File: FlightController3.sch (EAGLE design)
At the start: 38 parts, among them U1 NUCLEO_L432KC

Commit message: various improvements, mostly silkscreen labels
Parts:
- C13, C14: value (none) -> I2C
- C2: value AILERON_L -> AILERON L
- C3: value V_TAIL_L -> V-TAIL L
- C4: value V_TAIL_R -> V-TAIL R
- C5: value AILERON_R -> AILERON R
- INS1: value BNO055-BREAKOUT -> BNO055
- JP1, S1: value (none) -> RESET
- LED1: value (none) -> 5V
- LED2: value (none) -> 3V3
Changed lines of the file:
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@@
 <parts>
 <part name="C1" library="pinhead" deviceset="PINHD-1X3" device="" value="MOTOR"/>
-<part name="C2" library="pinhead" deviceset="PINHD-1X3" device="" value="AILERON_L"/>
-<part name="C5" library="pinhead" deviceset="PINHD-1X3" device="" value="AILERON_R"/>
-<part name="C3" library="pinhead" deviceset="PINHD-1X3" device="" value="V_TAIL_L"/>
-<part name="C4" library="pinhead" deviceset="PINHD-1X3" device="" value="V_TAIL_R"/>
+<part name="C2" library="pinhead" deviceset="PINHD-1X3" device="" value="AILERON L"/>
+<part name="C5" library="pinhead" deviceset="PINHD-1X3" device="" value="AILERON R"/>
+<part name="C3" library="pinhead" deviceset="PINHD-1X3" device="" value="V-TAIL L"/>
+<part name="C4" library="pinhead" deviceset="PINHD-1X3" device="" value="V-TAIL R"/>
 <part name="GND1" library="supply1" deviceset="GND" device=""/>
 <part name="P+1" library="supply1" deviceset="+5V" device=""/>
@@
 <part name="+3V3" library="supply1" deviceset="+3V3" device=""/>
 <part name="GND6" library="supply1" deviceset="GND" device=""/>
-<part name="INS1" library="1_Robo-Lib" deviceset="BNO055-BREAKOUT" device=""/>
+<part name="INS1" library="1_Robo-Lib" deviceset="BNO055-BREAKOUT" device="" value="BNO055"/>
 <part name="GND7" library="supply1" deviceset="GND" device=""/>
 <part name="MF1" library="BSN20_215" deviceset="BSN20,215" device=""/>
@@
 <part name="P+7" library="supply1" deviceset="+5V" device=""/>
 <part name="GND5" library="supply1" deviceset="GND" device=""/>
-<part name="C13" library="pinhead" deviceset="PINHD-1X4" device=""/>
-<part name="C14" library="pinhead" deviceset="PINHD-1X4" device=""/>
+<part name="C13" library="pinhead" deviceset="PINHD-1X4" device="" value="I2C"/>
+<part name="C14" library="pinhead" deviceset="PINHD-1X4" device="" value="I2C"/>
 <part name="FRAME1" library="frames" deviceset="A4L-LOC" device=""/>
 <part name="FRAME2" library="frames" deviceset="A4L-LOC" device=""/>
@@
 <part name="FRAME4" library="frames" deviceset="A4L-LOC" device=""/>
 <part name="U$1" library="toolbox" deviceset="TOOLBOX_LOGO" device=""/>
-<part name="JP1" library="pinhead" deviceset="PINHD-1X2" device=""/>
+<part name="JP1" library="pinhead" deviceset="PINHD-1X2" device="" value="RESET"/>
 <part name="GND8" library="supply1" deviceset="GND" device=""/>
-<part name="LED1" library="led" deviceset="LED" device="SML0603"/>
-<part name="LED2" library="led" deviceset="LED" device="SML0603"/>
+<part name="LED1" library="led" deviceset="LED" device="SML0603" value="5V"/>
+<part name="LED2" library="led" deviceset="LED" device="SML0603" value="3V3"/>
 <part name="+3V2" library="supply1" deviceset="+3V3" device=""/>
 <part name="P+8" library="supply1" deviceset="+5V" device=""/>
@@
 <part name="GND14" library="supply1" deviceset="GND" device=""/>
 <part name="GND15" library="supply1" deviceset="GND" device=""/>
-<part name="S1" library="switch-omron" deviceset="10-XX" device=""/>
+<part name="S1" library="switch-omron" deviceset="10-XX" device="" value="RESET"/>
 <part name="GND11" library="supply1" deviceset="GND" device=""/>
 <part name="U$2" library="toolbox" deviceset="TOOLBOX_LOGO" device=""/>

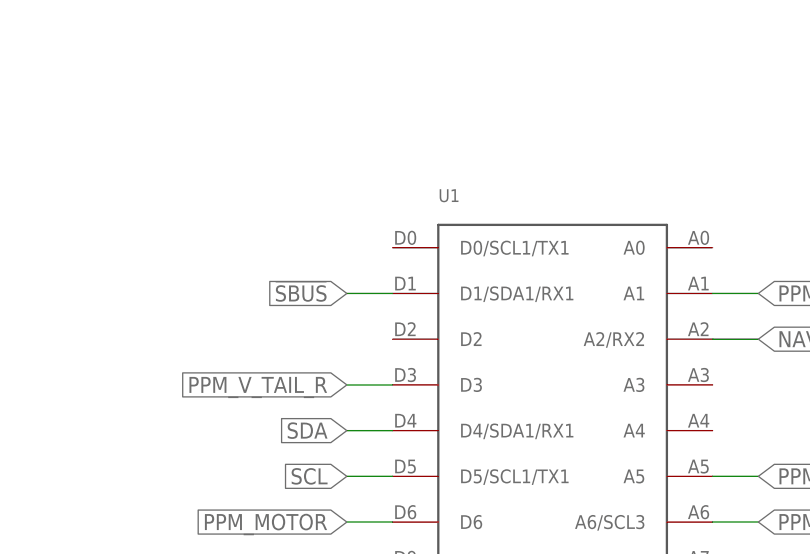
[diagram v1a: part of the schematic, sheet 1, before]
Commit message: fixed naming of D1/D0 and SBUS connection
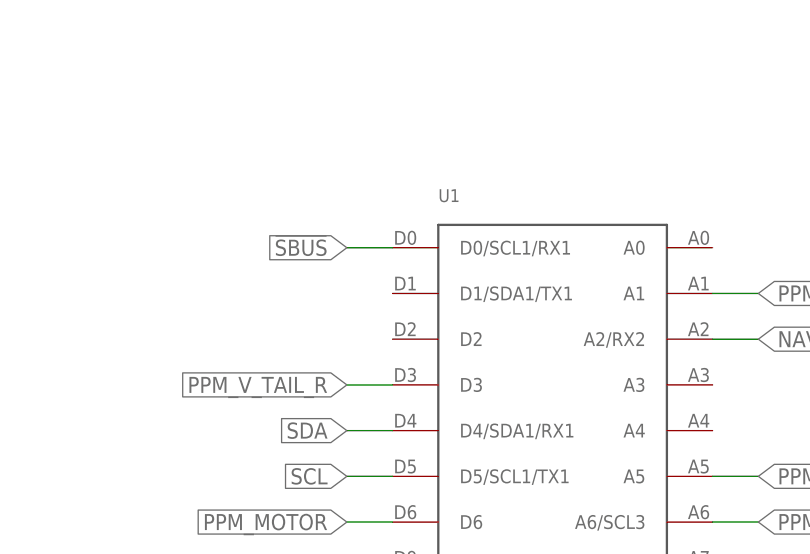
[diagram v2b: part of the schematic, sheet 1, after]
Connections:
- net !SBUS: now also U1.D0/SCL1/RX1; no longer U1.D1/SDA1/RX1
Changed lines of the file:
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@@
 <net name="!SBUS" class="0">
 <segment>
-<pinref part="U1" gate="G$1" pin="D1/SDA1/RX1"/>
-<wire x1="111.76" y1="132.08" x2="106.68" y2="132.08" width="0.1524" layer="91"/>
-<label x="106.68" y="132.08" size="1.778" layer="95" rot="R180" xref="yes"/>
+<label x="106.68" y="137.16" size="1.778" layer="95" rot="R180" xref="yes"/>
+<pinref part="U1" gate="G$1" pin="D0/SCL1/RX1"/>
+<wire x1="106.68" y1="137.16" x2="111.76" y2="137.16" width="0.1524" layer="91"/>
 </segment>
 </net>

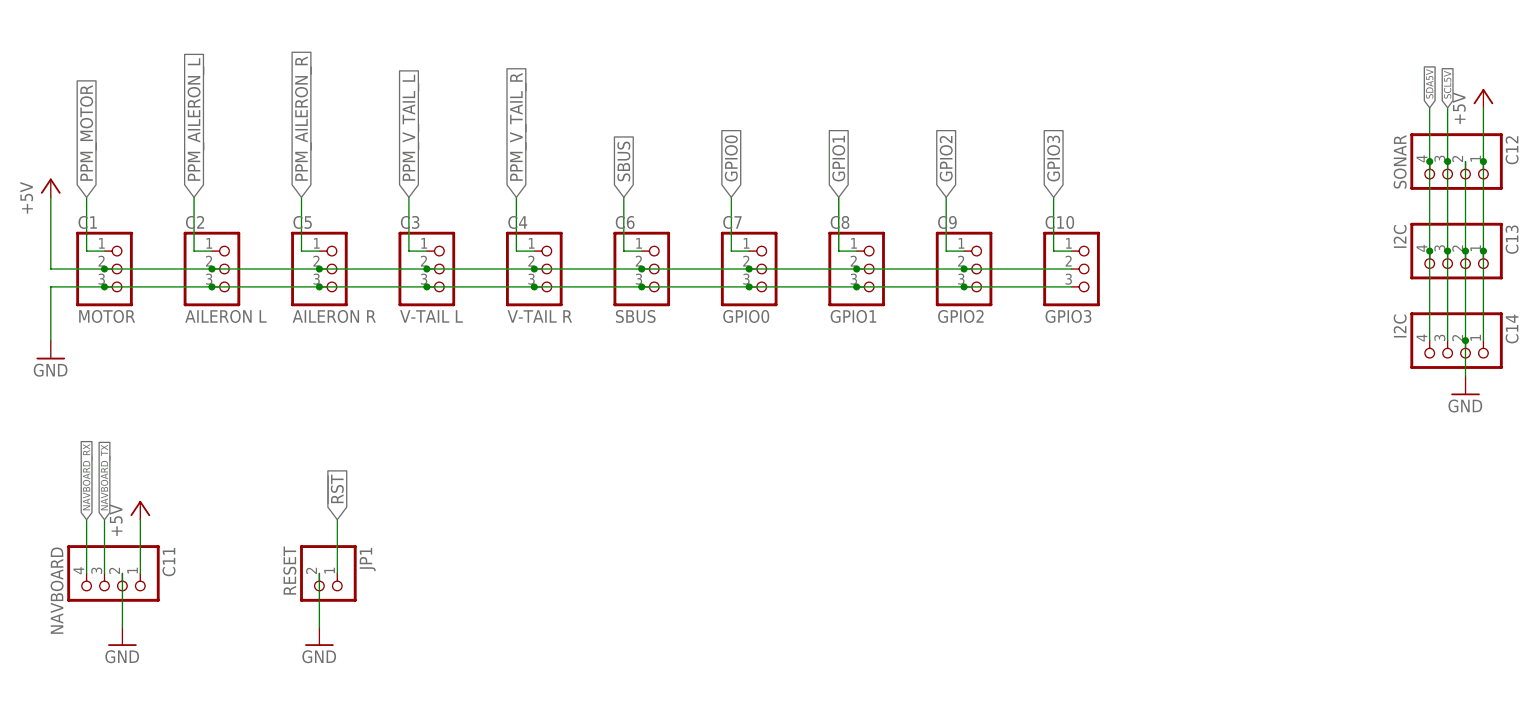
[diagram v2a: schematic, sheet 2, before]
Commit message: removed GPIO, I2C Ports, added expansion port
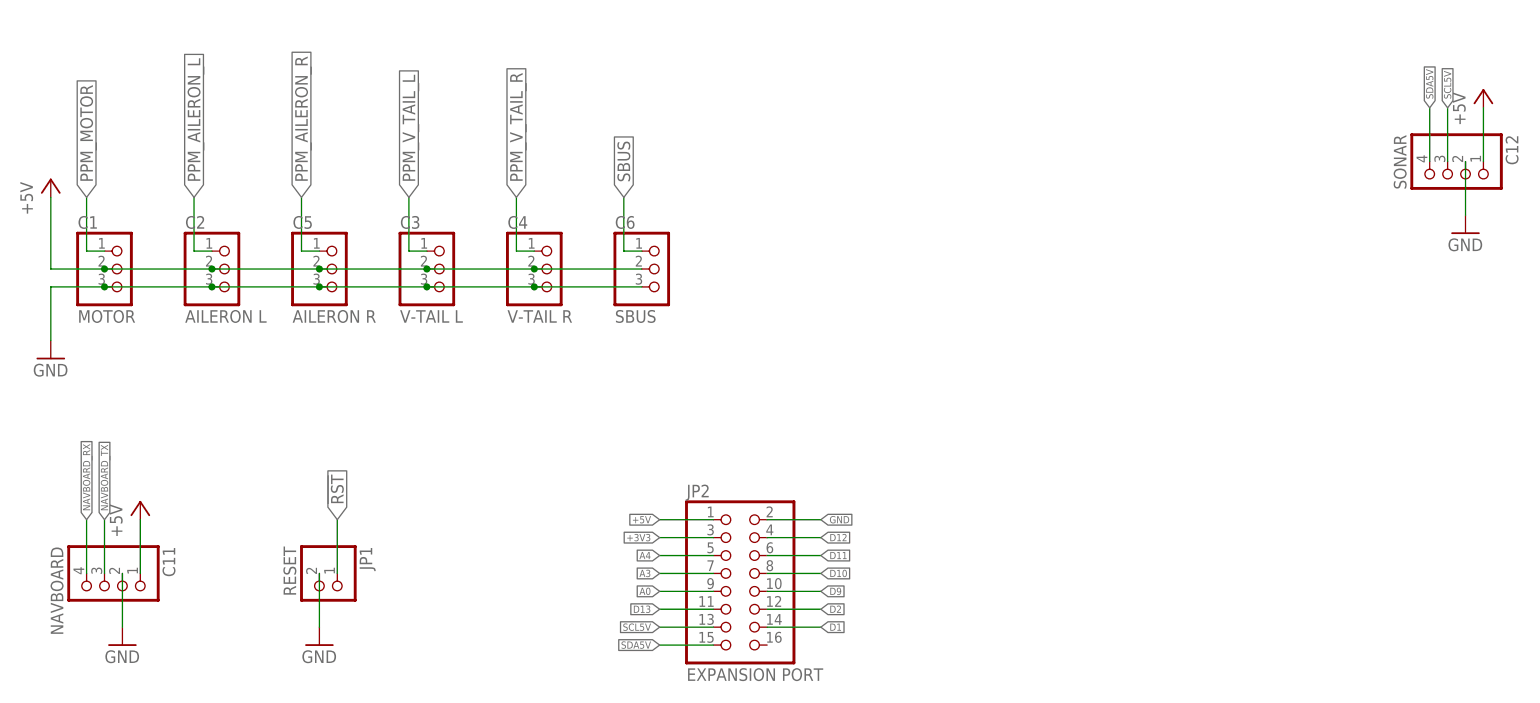
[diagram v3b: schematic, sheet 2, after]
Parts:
- removed C10: GPIO3, pinhead:PINHD-1X3
- removed C13, C14: I2C, pinhead:PINHD-1X4
- removed C7: GPIO0, pinhead:PINHD-1X3
- removed C8: GPIO1, pinhead:PINHD-1X3
- removed C9: GPIO2, pinhead:PINHD-1X3
- added JP2: EXPANSION PORT, pinhead:PINHD-2X8
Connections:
- removed net GPIO0: C7.1, U1.D9
- removed net GPIO1: C8.1, U1.D10
- removed net GPIO2: C9.1, U1.D11
- removed net GPIO3: C10.1, U1.D12/SDA3
- new net A0: JP2.9, U1.A0
- new net A3: JP2.7, U1.A3
- new net A4: JP2.5, U1.A4
- new net D1: JP2.14, U1.D1/SDA1/TX1
- new net D10: JP2.8, U1.D10
- new net D11: JP2.6, U1.D11
- new net D12: JP2.4, U1.D12/SDA3
- new net D13: JP2.11, U1.D13
- new net D2: JP2.12, U1.D2
- new net D9: JP2.10, U1.D9
- net +3V3: now also JP2.3
- net +5V: now also JP2.1; no longer C10.2, C13.1, C14.1, C7.2, C8.2, C9.2
- net GND: now also JP2.2; no longer C10.3, C13.2, C14.2, C7.3, C8.3, C9.3
- net SCL5V: now also JP2.13; no longer C13.3, C14.3
- net SDA5V: now also JP2.15; no longer C13.4, C14.4

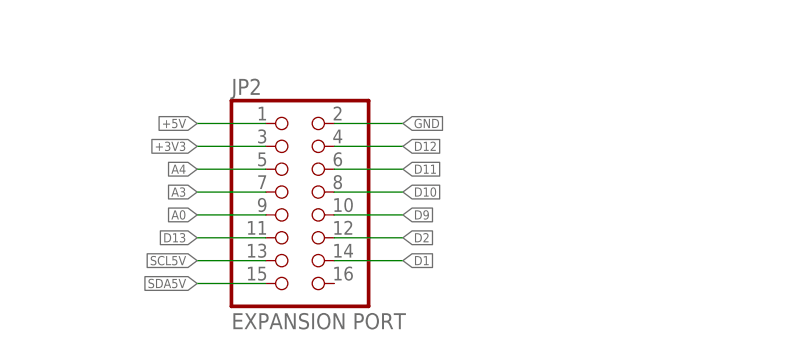
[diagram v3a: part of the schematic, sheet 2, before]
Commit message: smaller board footprint, added reset to port
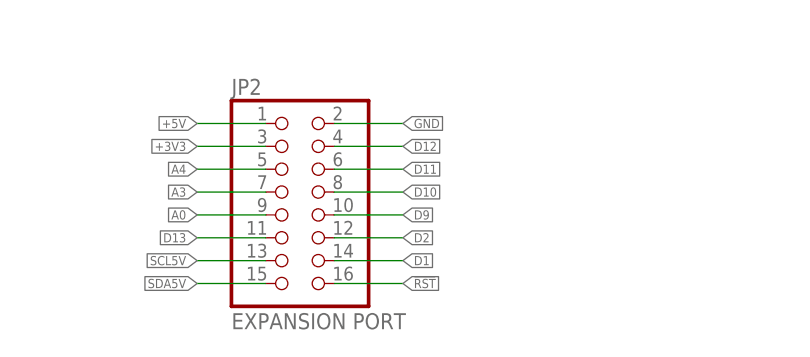
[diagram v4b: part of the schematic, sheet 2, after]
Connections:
- net !RST: now also JP2.16
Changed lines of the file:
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@@
 <label x="60.96" y="91.44" size="1.778" layer="95" rot="R90" xref="yes"/>
+</segment>
+<segment>
+<pinref part="JP2" gate="A" pin="16"/>
+<wire x1="121.92" y1="73.66" x2="129.54" y2="73.66" width="0.1524" layer="91"/>
+<label x="129.54" y="73.66" size="1.016" layer="95" xref="yes"/>
 </segment>
 </net>
